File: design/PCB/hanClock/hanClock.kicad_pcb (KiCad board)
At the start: 2 copper layers, 156.5 x 152.5 mm, 59 parts, among them J1 DHT22, J2 DS3231, J3 ←HC-06, Q1 BC547, SW1 mode_change_sw, SW2 ALARM_sw, SW3 TIME_sw, SW4 LED_sw

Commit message: PCB디자인 하는 중
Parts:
- added C0: 100nF, Capacitor_SMD:C_1206_3216Metric_Pad1.33x1.80mm_HandSolder, F.Cu at (-67.3, 28.8)
- added C1: 100nF, Capacitor_SMD:C_1206_3216Metric_Pad1.33x1.80mm_HandSolder, F.Cu at (-67.3, 32.1)
- added C10: 100nF, Capacitor_SMD:C_1206_3216Metric_Pad1.33x1.80mm_HandSolder, F.Cu at (-49.3, 28.8)
- added C11: 100nF, Capacitor_SMD:C_1206_3216Metric_Pad1.33x1.80mm_HandSolder, F.Cu at (-67.3, 45.5)
- added C12: 100nF, Capacitor_SMD:C_1206_3216Metric_Pad1.33x1.80mm_HandSolder, F.Cu at (-61.3, 38.8)
- added C13: 100nF, Capacitor_SMD:C_1206_3216Metric_Pad1.33x1.80mm_HandSolder, F.Cu at (-55.3, 35.5)
- added C14: 100nF, Capacitor_SMD:C_1206_3216Metric_Pad1.33x1.80mm_HandSolder, F.Cu at (-49.3, 32.1)
- added C15: 100nF, Capacitor_SMD:C_1206_3216Metric_Pad1.33x1.80mm_HandSolder, F.Cu at (-61.3, 42.2)
- added C16: 100nF, Capacitor_SMD:C_1206_3216Metric_Pad1.33x1.80mm_HandSolder, F.Cu at (-67.3, 48.9)
- added C17: 100nF, Capacitor_SMD:C_1206_3216Metric_Pad1.33x1.80mm_HandSolder, F.Cu at (-43.3, 28.8)
- added C18: 100nF, Capacitor_SMD:C_1206_3216Metric_Pad1.33x1.80mm_HandSolder, F.Cu at (-61.3, 45.5)
- added C19: 100nF, Capacitor_SMD:C_1206_3216Metric_Pad1.33x1.80mm_HandSolder, F.Cu at (-55.3, 38.8)
- added C2: 100nF, Capacitor_SMD:C_1206_3216Metric_Pad1.33x1.80mm_HandSolder, F.Cu at (-61.3, 28.8)
- added C20: 100nF, Capacitor_SMD:C_1206_3216Metric_Pad1.33x1.80mm_HandSolder, F.Cu at (-49.3, 35.5)
- added C21: 100nF, Capacitor_SMD:C_1206_3216Metric_Pad1.33x1.80mm_HandSolder, F.Cu at (-43.3, 32.1)
- added C22: 100nF, Capacitor_SMD:C_1206_3216Metric_Pad1.33x1.80mm_HandSolder, F.Cu at (-55.3, 42.2)
- added C23: 100nF, Capacitor_SMD:C_1206_3216Metric_Pad1.33x1.80mm_HandSolder, F.Cu at (-61.3, 48.9)
- added C24: 100nF, Capacitor_SMD:C_1206_3216Metric_Pad1.33x1.80mm_HandSolder, F.Cu at (-37.2, 28.8)
- added C25: 100nF, Capacitor_SMD:C_1206_3216Metric_Pad1.33x1.80mm_HandSolder, F.Cu at (-55.3, 45.5)
- added C26: 100nF, Capacitor_SMD:C_1206_3216Metric_Pad1.33x1.80mm_HandSolder, F.Cu at (-49.3, 38.8)
- added C27: 100nF, Capacitor_SMD:C_1206_3216Metric_Pad1.33x1.80mm_HandSolder, F.Cu at (-43.3, 35.5)
- added C28: 100nF, Capacitor_SMD:C_1206_3216Metric_Pad1.33x1.80mm_HandSolder, F.Cu at (-37.2, 32.1)
- added C29: 100nF, Capacitor_SMD:C_1206_3216Metric_Pad1.33x1.80mm_HandSolder, F.Cu at (-49.3, 42.2)
- added C3: 100nF, Capacitor_SMD:C_1206_3216Metric_Pad1.33x1.80mm_HandSolder, F.Cu at (-67.3, 35.5)
- added C30: 100nF, Capacitor_SMD:C_1206_3216Metric_Pad1.33x1.80mm_HandSolder, F.Cu at (-55.3, 48.9)
- added C31: 100nF, Capacitor_SMD:C_1206_3216Metric_Pad1.33x1.80mm_HandSolder, F.Cu at (-31.2, 28.8)
- added C32: 100nF, Capacitor_SMD:C_1206_3216Metric_Pad1.33x1.80mm_HandSolder, F.Cu at (-49.3, 45.5)
- added C33: 100nF, Capacitor_SMD:C_1206_3216Metric_Pad1.33x1.80mm_HandSolder, F.Cu at (-43.3, 38.8)
- added C34: 100nF, Capacitor_SMD:C_1206_3216Metric_Pad1.33x1.80mm_HandSolder, F.Cu at (-37.2, 35.5)
- added C4: 100nF, Capacitor_SMD:C_1206_3216Metric_Pad1.33x1.80mm_HandSolder, F.Cu at (-61.3, 32.1)
- added C5: 100nF, Capacitor_SMD:C_1206_3216Metric_Pad1.33x1.80mm_HandSolder, F.Cu at (-55.3, 28.8)
- added C6: 100nF, Capacitor_SMD:C_1206_3216Metric_Pad1.33x1.80mm_HandSolder, F.Cu at (-67.3, 38.8)
- added C7: 100nF, Capacitor_SMD:C_1206_3216Metric_Pad1.33x1.80mm_HandSolder, F.Cu at (-61.3, 35.5)
- added C8: 100nF, Capacitor_SMD:C_1206_3216Metric_Pad1.33x1.80mm_HandSolder, F.Cu at (-55.3, 32.1)
- added C9: 100nF, Capacitor_SMD:C_1206_3216Metric_Pad1.33x1.80mm_HandSolder, F.Cu at (-67.3, 42.2)
- added R10: 110Ω, Resistor_SMD:R_1206_3216Metric_Pad1.30x1.75mm_HandSolder, F.Cu at (73.1, 42.9)
- added R11: 110Ω, Resistor_SMD:R_1206_3216Metric_Pad1.30x1.75mm_HandSolder, F.Cu at (67.1, 49.6)
- added R12: 110Ω, Resistor_SMD:R_1206_3216Metric_Pad1.30x1.75mm_HandSolder, F.Cu at (61.1, 56.2)
- added R13: 110Ω, Resistor_SMD:R_1206_3216Metric_Pad1.30x1.75mm_HandSolder, F.Cu at (67.1, 52.9)
- added R5: 110Ω, Resistor_SMD:R_1206_3216Metric_Pad1.30x1.75mm_HandSolder, F.Cu at (73.1, 39.6)
- added R6: 110Ω, Resistor_SMD:R_1206_3216Metric_Pad1.30x1.75mm_HandSolder, F.Cu at (61.1, 49.6)
- added R7: 110Ω, Resistor_SMD:R_1206_3216Metric_Pad1.30x1.75mm_HandSolder, F.Cu at (55.1, 56.3)
- added R8: 110Ω, Resistor_SMD:R_1206_3216Metric_Pad1.30x1.75mm_HandSolder, F.Cu at (61.1, 52.9)
- added R9: 110Ω, Resistor_SMD:R_1206_3216Metric_Pad1.30x1.75mm_HandSolder, F.Cu at (67.1, 46.3)
- A1: value Arduino_Nano_v3.x -> Arduino_Nano_v3.1
- D0, D1, D10, D11, D12, D13, D14, D15, D16, D17, D18, D19, D2, D20, D21, D22, D23, D24, D25, D26, D27, D28, D29, D3, D30, D31, D32, D33, D34, D4, D5, D6, D7, D8, D9: footprint parts:LED_SK6812_PLCC4_5.0x5.0mm_P3.2mm -> LED_SMD:LED_SK6812_PLCC4_5.0x5.0mm_P3.2mm
- J1: value DHT22 -> DHT22-11
- J3: value ←HC-06 -> HM-10
- SW2: value ALARM_sw -> Time_sw
- SW3: value TIME_sw -> LED_sw
- SW4: value LED_sw -> Alarm_sw
- renumbered C1 to C35
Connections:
- D17 pad 1: GND -> Net-(D17-Pad1)
- D18 pad 1: GND -> Net-(D18-Pad1)
- D19 pad 1: GND -> Net-(D19-Pad1)
- D20 pad 1: GND -> Net-(D20-Pad1)
- D21 pad 1: GND -> Net-(D21-Pad1)
- D22 pad 1: GND -> Net-(D22-Pad1)
- D35 pad 1: GND -> Net-(D35-Pad1)
- D36 pad 1: GND -> Net-(D36-Pad1)
- D37 pad 1: GND -> Net-(D37-Pad1)
- D38 pad 1: GND -> Net-(D38-Pad1)
- D39 pad 1: GND -> Net-(D39-Pad1)
- D40 pad 1: GND -> Net-(D40-Pad1)
- D41 pad 1: GND -> Net-(D41-Pad1)
- D42 pad 1: GND -> Net-(D42-Pad1)
- D43 pad 1: GND -> Net-(D43-Pad1)
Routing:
- net +5V: track 1286.3 -> 312.7 mm, vias 6 -> 1
- net GND: track 1540.4 -> 817.7 mm, vias 6 -> 4
- net Net-(D19-Pad4): track 38.8 -> 0.00 mm
- net Net-(D7-Pad4): track 35.6 -> 0.00 mm
- net Net-(D31-Pad4): track 35.6 -> 0.04 mm
- net Net-(D32-Pad4): track 34.1 -> 0.04 mm
- net Net-(D25-Pad4): track 32.7 -> 0.00 mm
- net Net-(D4-Pad4): track 32.2 -> 0.00 mm, vias 2 -> 0
- net Net-(D33-Pad4): track 31.7 -> 0.00 mm
- net Net-(D21-Pad4): track 31.6 -> 0.00 mm
- net Net-(D17-Pad4): track 31.6 -> 0.00 mm
- net Net-(D20-Pad4): track 31.6 -> 0.00 mm
- net Net-(D18-Pad4): track 31.6 -> 0.00 mm
- net Net-(D10-Pad2): track 31.6 -> 0.00 mm
- net Net-(D30-Pad4): track 31.6 -> 0.00 mm
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
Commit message: Revise PCB design
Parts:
- added R14: 10KΩ, Resistor_THT:R_Axial_DIN0207_L6.3mm_D2.5mm_P10.16mm_Horizontal, B.Cu at (88.3, 123.7)
- moved C0 243.4 mm to (149.8, 138.9), turned to 90 degrees
- moved C1 219.4 mm to (124.4, 138.9), turned to 90 degrees
- moved C11 216.8 mm to (143.8, 95.0)
- moved C10 213.7 mm to (143.8, 120.4), turned to 180 degrees
- moved C9 204.5 mm to (124.4, 113.5), turned to 270 degrees
- moved C23 199.3 mm to (137.8, 39.0), turned to 90 degrees
- moved C22 194.8 mm to (138.2, 64.5), turned to 270 degrees
- moved C2 194.4 mm to (99.0, 138.9), turned to 90 degrees
- moved C12 192.1 mm to (124.4, 88.1), turned to 90 degrees
- moved C34 181.7 mm to (143.8, 19.5), turned to 180 degrees
- moved C8 174.4 mm to (99.0, 113.5), turned to 270 degrees
- moved C3 171.5 mm to (69.5, 138.9), turned to 90 degrees
- moved C33 170.4 mm to (125.0, 11.8), turned to 270 degrees
- moved C21 170.4 mm to (124.4, 62.6), turned to 270 degrees
- moved C13 162.3 mm to (98.3, 88.1), turned to 90 degrees
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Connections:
- D17 pad 1: Net-(D17-Pad1) -> GND
- D18 pad 1: Net-(D18-Pad1) -> GND
- D19 pad 1: Net-(D19-Pad1) -> GND
- D20 pad 1: Net-(D20-Pad1) -> GND
- D21 pad 1: Net-(D21-Pad1) -> GND
- D22 pad 1: Net-(D22-Pad1) -> GND
- Q1 pad 2: Net-(A1-Pad6) -> Net-(Q1-Pad2)
- R2 pad 2: GND -> +5V
- R4 pad 1: +5V -> GND
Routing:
- net +5V: track 312.7 -> 1426.2 mm, vias 1 -> 2
- net GND: track 817.7 -> 1655.6 mm, vias 4 -> 3
- net Net-(D4-Pad4): track 0.00 -> 43.7 mm
- net Net-(D39-Pad1): track 0.41 -> 41.8 mm
- net Net-(D3-Pad4): track 0.04 -> 30.0 mm
- net Net-(D7-Pad4): track 0.00 -> 28.2 mm
- net Net-(D25-Pad4): track 0.00 -> 28.2 mm
- net Net-(D19-Pad4): track 0.00 -> 28.2 mm
- net Net-(D13-Pad4): track 0.00 -> 28.2 mm
- net Net-(D31-Pad4): track 0.04 -> 28.2 mm
- net Net-(D2-Pad4): track 0.18 -> 28.2 mm
- net Net-(D28-Pad4): track 0.00 -> 27.2 mm
- net Net-(D22-Pad4): track 0.00 -> 26.9 mm
- net Net-(D16-Pad4): track 0.00 -> 26.9 mm
- net Net-(D10-Pad4): track 0.00 -> 26.6 mm
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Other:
- board text added: "Made by gogomaker HangeulClock v2"
- board text removed: "Made by gogomaker HnageulClock v2"
- board text removed: "VCC"

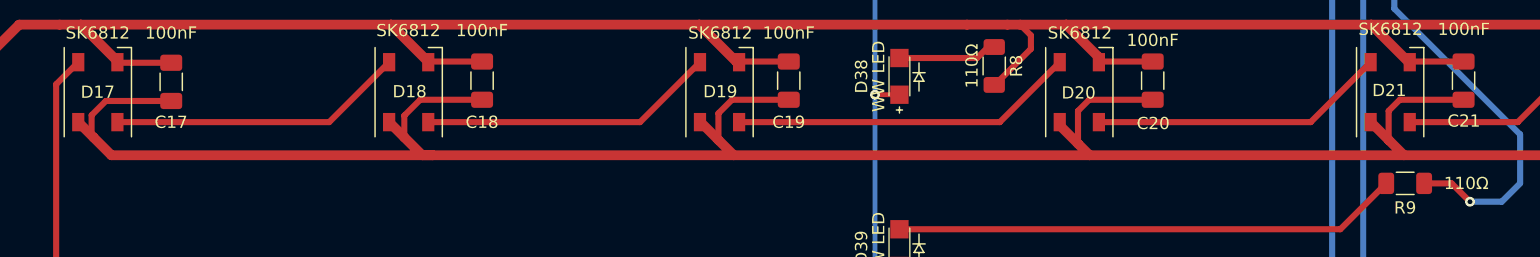
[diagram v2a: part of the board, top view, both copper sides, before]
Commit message: LED출력코드 수정완료 LED출력하는 주소값들을 모두 수정 완료하였다
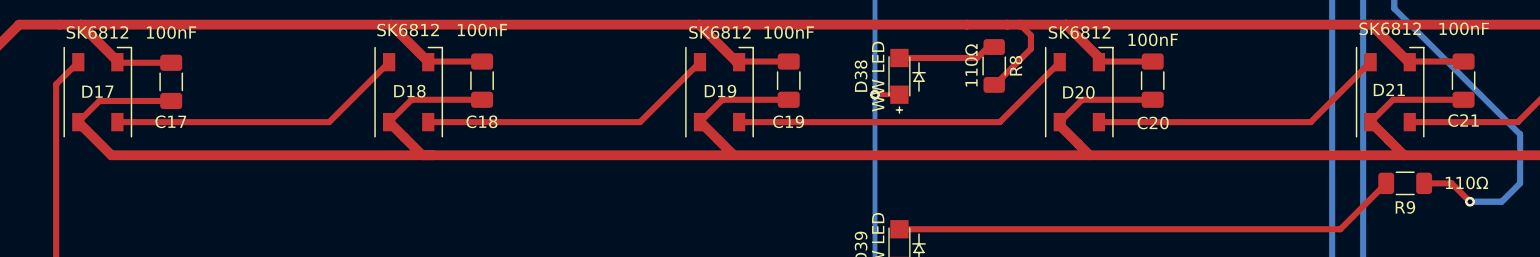
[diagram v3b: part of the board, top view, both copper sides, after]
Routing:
- net +5V: track 1426.2 -> 1423.6 mm

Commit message: Resync files 컴퓨터 갈아엎으면서 바뀐 파일 등 기타 모든 파일들 일괄 커밋
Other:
- net class Default removed
